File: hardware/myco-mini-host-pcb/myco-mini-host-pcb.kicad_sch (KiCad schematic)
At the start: 34 parts, among them J1 Conn_01x17_Female, J2 Conn_01x17_Female, Q1 AO3401A, Q2 AO3401A, Q3 AO3401A, Q4 AO3401A, SW1 DM-04-V, SW2 TS-1187A-B-A-B, U1 XC9145B33CMR-G, U2 SHT41-AD1B-R2, U3 BH1750FVI-TR, U4 MAX40203AUK+T

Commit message: fix: boost toujours actif (CE->VDD_NRF), modeles 3D, regles JLCPCB
- CE du XC9145 cable en dur sur VDD_NRF au lieu d'une GPIO : le boost
  alimente maintenant le nRF54 lui-meme, plus aucun scenario ou le
  firmware voudrait legitimement le couper (couperait sa propre
  alim) - supprime aussi le risque de brick si cette GPIO avait ete
  mise a l'etat bas par erreur
- R6 (pull-down CE) retire, plus necessaire - le tie direct satisfait
  deja l'exigence datasheet "ne pas laisser CE flottant"
- P1.05 redevient libre (broche J1 pin13)
- fix regression : label C2 revenu sur VDD_NRF au lieu de VOUT_3V3
  entre deux etapes precedentes (cause non identifiee avec certitude,
  isole aux 8 autres renommages de la meme tache qui etaient intacts)
- chemins de modeles 3D corriges sur les 8 footprints custom
  (${KIPRJMOD}/libs/... au lieu d'un chemin absolu casse)
- modeles 3D ajoutes pour U1 (XC9145, generique SOT-23-5 - LCSC n'a
  aucun modele pour ce package) et D1 (LED RGB 5050-6, meme raison)
- regles de conception resserrees pour matcher les minimums JLCPCB
  (min_clearance, min_via_diameter, min_via_annular_width,
  min_hole_to_hole) - geometrie actuelle du board deja conforme,
  DRC toujours propre apres resserrement
- placement/routage PCB (travail manuel utilisateur)

Co-Authored-By: Claude Sonnet 5 <noreply@anthropic.com>
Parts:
- removed R6: 100k, Resistor_SMD:R_0603_1608Metric, symbol Device:R
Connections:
- net VDD_NRF: now also U1.1 (CE)
- net P1_05_BOOST_EN: no longer names the net of J1.13 (Pin_13)
- net P1_05_BOOST_EN: no longer U1.1 (CE)
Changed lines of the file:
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@@
 	(wire
 		(pts
-			(xy 250.19 66.04) (xy 250.19 62.23)
-		)
-		(stroke
-			(width 0)
-			(type default)
-		)
-	)
-	(wire
-		(pts
 			(xy 34.29 69.85) (xy 30.48 69.85)
 		)
@@
 	(wire
 		(pts
+			(xy 34.29 107.95) (xy 30.48 107.95)
+		)
+		(stroke
+			(width 0)
+			(type default)
+		)
+	)
+	(wire
+		(pts
 			(xy 360.68 154.94) (xy 364.49 154.94)
 		)
@@
 	(wire
 		(pts
-			(xy 250.19 73.66) (xy 250.19 77.47)
-		)
-		(stroke
-			(width 0)
-			(type default)
-		)
-	)
-	(wire
-		(pts
 			(xy 370.84 250.19) (xy 367.03 250.19)
 		)
@@
 	(wire
 		(pts
-			(xy 34.29 100.33) (xy 30.48 100.33)
-		)
-		(stroke
-			(width 0)
-			(type default)
-		)
-	)
-	(wire
-		(pts
 			(xy 350.52 246.38) (xy 350.52 242.57)
 		)
@@
 		)
 	)
-	(wire
-		(pts
-			(xy 34.29 107.95) (xy 30.48 107.95)
-		)
-		(stroke
-			(width 0)
-			(type default)
-		)
-	)
 	(label "SENSOR_3V3"
 		(at 129.54 92.71 0)
@@
 		)
 	)
-	(label "P1_10_SDA"
-		(at 22.86 74.93 0)
+	(label "VDD_NRF"
+		(at 199.39 31.75 0)
 		(effects
 			(font
@@
 		)
 	)
-	(label "LED_B_NODE"
-		(at 367.03 246.38 0)
+	(label "P1_10_SDA"
+		(at 22.86 74.93 0)
 		(effects
 			(font
@@
 		)
 	)
-	(label "P1_05_BOOST_EN"
-		(at 250.19 62.23 0)
+	(label "LED_B_NODE"
+		(at 367.03 246.38 0)
 		(effects
 			(font
@@
 		)
 	)
-	(label "P1_05_BOOST_EN"
+	(label "VDD_NRF"
 		(at 236.22 41.91 0)
 		(effects
@@
 		)
 	)
-	(label "P1_05_BOOST_EN"
-		(at 30.48 100.33 0)
-		(effects
-			(font
-				(size 1.27 1.27)
-			)
-			(justify left bottom)
-		)
-	)
 	(label "P2_06_LED_B"
 		(at 16.51 195.58 0)
@@
 		)
 	)
+	(label "P1_08_SOIL_SW"
+		(at 30.48 107.95 0)
+		(effects
+			(font
+				(size 1.27 1.27)
+			)
+			(justify left bottom)
+		)
+	)
 	(label "VDD_PROT"
 		(at 165.1 69.85 0)
@@
 		)
 	)
-	(label "VDD_NRF"
-		(at 199.39 31.75 0)
-		(effects
-			(font
-				(size 1.27 1.27)
-			)
-			(justify left bottom)
-		)
-	)
 	(label "P2_03_DIP3"
 		(at 30.48 203.2 0)
@@
 		)
 	)
-	(label "P1_08_SOIL_SW"
-		(at 30.48 107.95 0)
-		(effects
-			(font
-				(size 1.27 1.27)
-			)
-			(justify left bottom)
-		)
-	)
 	(symbol
 		(lib_id "power:GND")
@@
 	(symbol
 		(lib_id "Device:R")
-		(at 250.19 69.85 0)
-		(unit 1)
-		(body_style 1)
-		(exclude_from_sim no)
-		(in_bom yes)
-		(on_board yes)
-		(in_pos_files yes)
-		(dnp no)
-		(property "Reference" "R6"
-			(at 250.19 63.85 0)
-			(show_name no)
-			(do_not_autoplace no)
-			(effects
-				(font
-					(size 1.27 1.27)
-				)
-			)
-		)
-		(property "Value" "100k"
-			(at 250.19 75.85 0)
-			(show_name no)
-			(do_not_autoplace no)
-			(effects
-				(font
-					(size 1.27 1.27)
-				)
-			)
-		)
-		(property "Footprint" "Resistor_SMD:R_0603_1608Metric"
-			(at 250.19 69.85 0)
-			(hide yes)
-			(show_name no)
-			(do_not_autoplace no)
-			(effects
-				(font
-					(size 1.27 1.27)
-				)
-			)
-		)
-		(property "Datasheet" ""
-			(at 250.19 69.85 0)
-			(show_name no)
-			(do_not_autoplace no)
-			(effects
-				(font
-					(size 1.27 1.27)
-				)
-			)
-		)
-		(property "Description" ""
-			(at 250.19 69.85 0)
-			(show_name no)
-			(do_not_autoplace no)
-			(effects
-				(font
-					(size 1.27 1.27)
-				)
-			)
-		)
-		(property "Note" "CE pull-down - datasheet: do not leave CE open"
-			(at 250.19 69.85 0)
-			(hide yes)
-			(show_name no)
-			(do_not_autoplace no)
-			(effects
-				(font
-					(size 1.27 1.27)
-				)
-			)
-		)
-		(pin "1"
-		)
-		(pin "2"
-		)
-		(instances
-			(project "myco-mini-host-pcb"
-				(path "/b1969cb4-f84b-4d7e-8508-ab863aa656b2"
-					(reference "R6")
-					(unit 1)
-				)
-			)
-		)
-	)
-	(symbol
-		(lib_id "Device:R")
 		(at 412.75 114.3 0)
 		(unit 1)
@@
 					(unit 1)
 				)
-			)
-		)
-	)
-	(symbol
-		(lib_id "power:GND")
-		(at 250.19 77.47 0)
-		(unit 1)
-		(body_style 1)
-		(exclude_from_sim no)
-		(in_bom yes)
-		(on_board yes)
-		(in_pos_files yes)
-		(dnp no)
-		(property "Reference" "#PWR10"
-			(at 250.19 83.47 0)
-			(hide yes)
-			(show_name no)
-			(do_not_autoplace no)
-			(effects
-				(font
-					(size 1.27 1.27)
-				)
-			)
-		)
-		(property "Value" "GND"
-			(at 250.19 81.47 0)
-			(show_name no)
-			(do_not_autoplace no)
-			(effects
-				(font
-					(size 1.27 1.27)
-				)
-			)
-		)
-		(property "Footprint" ""
-			(at 250.19 77.47 0)
-			(hide yes)
-			(show_name no)
-			(do_not_autoplace no)
-			(effects
-				(font
-					(size 1.27 1.27)
-				)
-			)
-		)
-		(property "Datasheet" ""
-			(at 250.19 77.47 0)
-			(show_name no)
-			(do_not_autoplace no)
-			(effects
-				(font
-					(size 1.27 1.27)
-				)
-			)
-		)
-		(property "Description" ""
-			(at 250.19 77.47 0)
-			(show_name no)
-			(do_not_autoplace no)
-			(effects
-				(font
-					(size 1.27 1.27)
-				)
-			)
-		)
-		(pin "1"
-		)
-		(instances
-			(project "myco-mini-host-pcb"
-				(path "/b1969cb4-f84b-4d7e-8508-ab863aa656b2"
-					(reference "#PWR10")
-					(unit 1)
-				)

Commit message: chore: snapshot avant corrections audit #2 (passe manuelle utilisateur)
Etat du schema et du PCB apres la passe manuelle de l'utilisateur
(alignement des textes/labels pour qu'ils ne chevauchent plus les
symboles, placement/routage PCB), avant d'appliquer les corrections
remontees par le second audit Opus 5.

Point de retour propre pour les corrections a venir :
- Q1 (protection inversion polarite) oriente a l'envers
- pas de decouplage sur SENSOR_3V3
- pas de pull-up sur P1_12_SENSOR_EN (Q3/Q4 flottants au boot)
- LED rouge/vert croisees, stubs I2C orphelins
- BOM obsolete (R6 fantome, commentaire R11/R12)
- VDD_NRF mal nomme (n'alimente plus le nRF54)

Co-Authored-By: Claude Sonnet 5 <noreply@anthropic.com>
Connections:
- net LED_B_NODE: no longer names the net of D1.1 (B), R9.1
- net LED_G_NODE: no longer names the net of D1.3 (G), R8.1
- net LED_R_NODE: no longer names the net of D1.2 (R), R7.1
- no-connect marks 0 -> 15
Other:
- note removed: "J1 = recepteur breakout J1 'GPIO_L' (1x17, 2.54mm)"
- note removed: "J2 = recepteur breakout J4 'GPIO_R' (1x17, 2.54mm)"
- note removed: "Pins headers non utilisees dans ce brouillon = laissees non cablees (GPIO libres, voir docs/host-pcb-design-brief.md)"
- moved on the sheet: D1, J1, J2, L1, R7, R8, R9, SW1

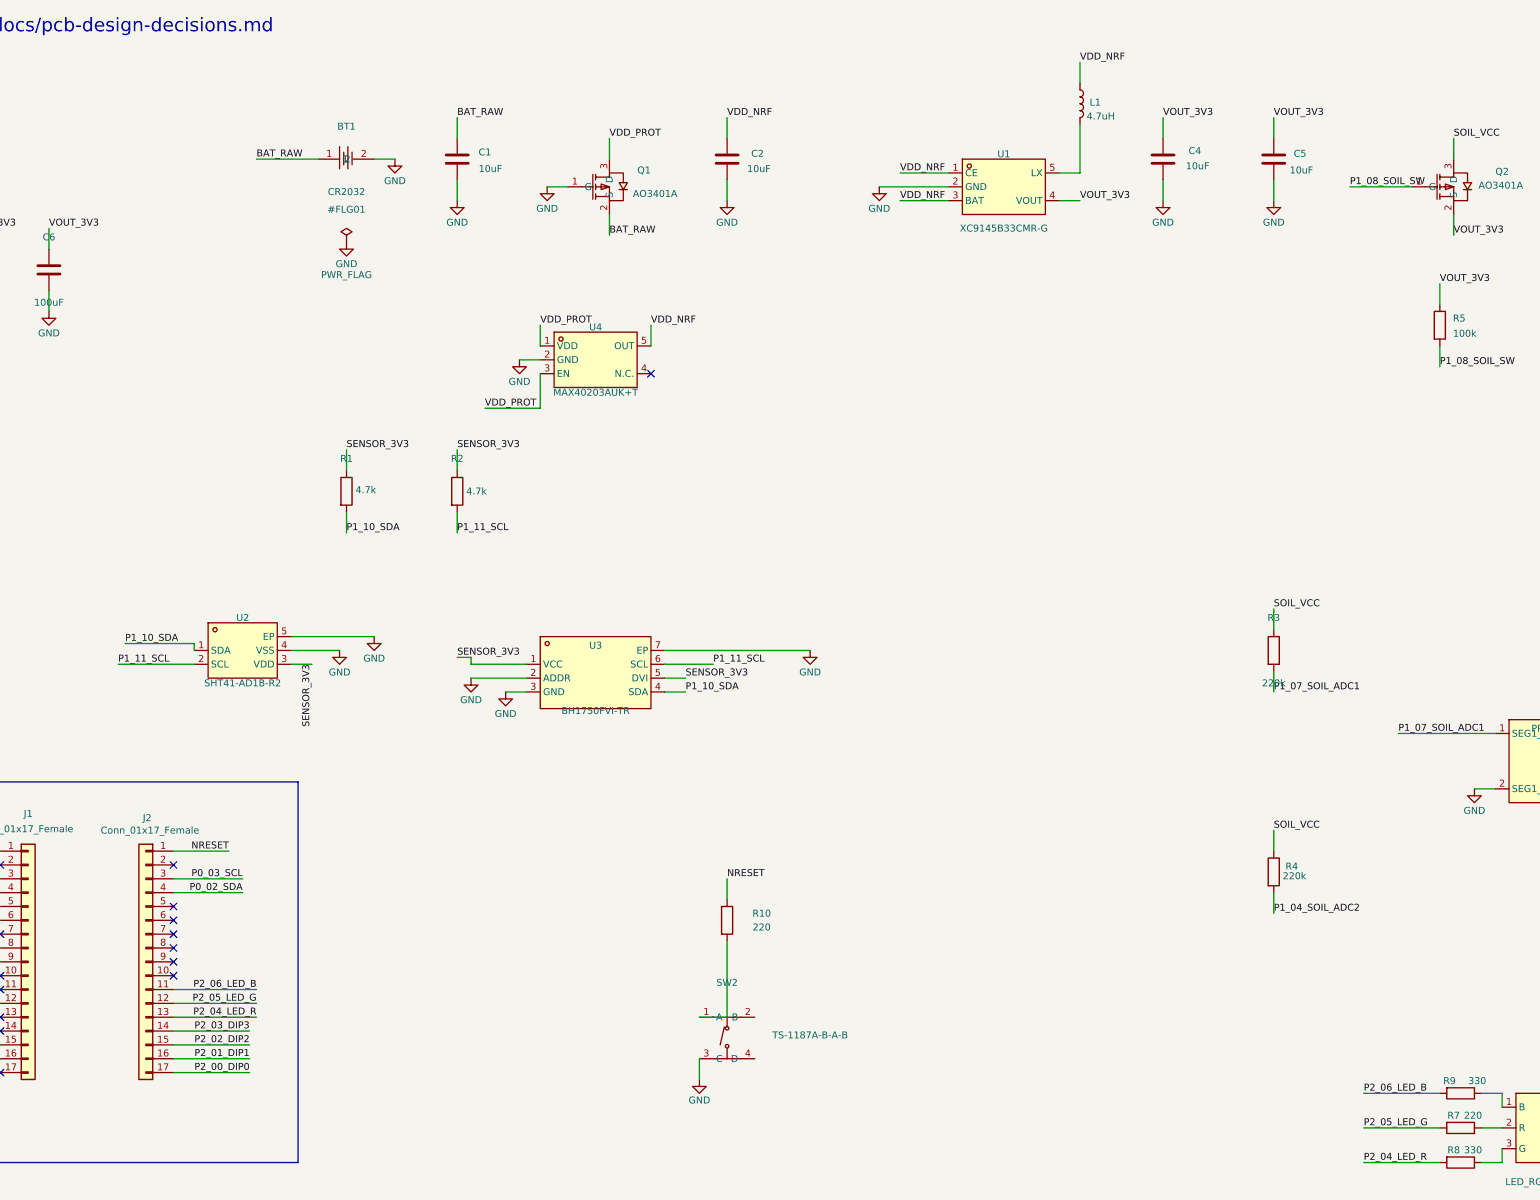
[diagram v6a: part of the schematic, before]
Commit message: fix: Q1 oriente a l'envers (aucune protection inversion), decouplage, garde-fous
Corrections du second audit Opus 5. Schema uniquement, le PCB reste a
l'utilisateur.

CRITIQUE - Q1 (protection inversion polarite) etait cable a l'envers :
  S=BAT_RAW / D=VDD_PROT, soit le motif "load switch" de Q2/Q3/Q4 (correct
  pour EUX, faux ici). Sur un P-FET la diode de corps a anode=Drain : avec
  la Source cote pile, une pile inseree a l'envers laisse cette diode
  PASSANTE, donc zero protection, et U4 (max absolu -0.3V) verrait ~-2.3V.
  Repere decisif : dans un montage correct la diode de corps conduit en
  fonctionnement NORMAL (elle amorce la charge, le canal la court-circuite
  ensuite) et ne bloque qu'a l'inversion. Corrige en D=BAT_RAW / S=VDD_PROT
  (echange des deux labels, aucune modif de geometrie). Brochage AO3401A
  reverifie sur datasheet (1=G, 2=S, 3=D). NB: le brief sec.4 contient
  toujours la meme erreur ("Source -> CR2032+"), d'ou le passage au travers
  du premier audit qui validait la conformite au brief, pas la physique.

Autres corrections :
- C7/C8 (100nF) + C9 (1uF) sur SENSOR_3V3 : le rail commute par Q3 n'avait
  aucune capacite locale, tout le decouplage etant reste en amont sur
  VOUT_3V3. ROHM specifie 0.1uF sur le VCC du BH1750, Sensirion l'exige
  pour le SHT4x, et ce rail se recharge depuis zero a chaque mesure.
- R13 (100k) sur P1_12_SENSOR_EN : les grilles de Q3/Q4 flottaient au boot
  (boost desormais toujours actif => VOUT_3V3 vivant avant que la GPIO ne
  sorte de haute impedance). Meme role que R5 pour Q2.
- LED rouge/vert : les noms de net etaient croises par rapport aux puces
  reellement atteintes. Valeurs des resistances deja correctes par couleur
  (220R sur le rouge), donc seuls les noms bougent.
- VDD_NRF -> BOOST_IN : ce net n'alimente plus le nRF54 depuis que J1 pin9
  est passe sur VOUT_3V3, c'est le rail d'entree du boost.
- Stubs I2C orphelins P0_02_SDA / P0_03_SCL supprimes, remplaces par des
  no-connect comme les autres br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
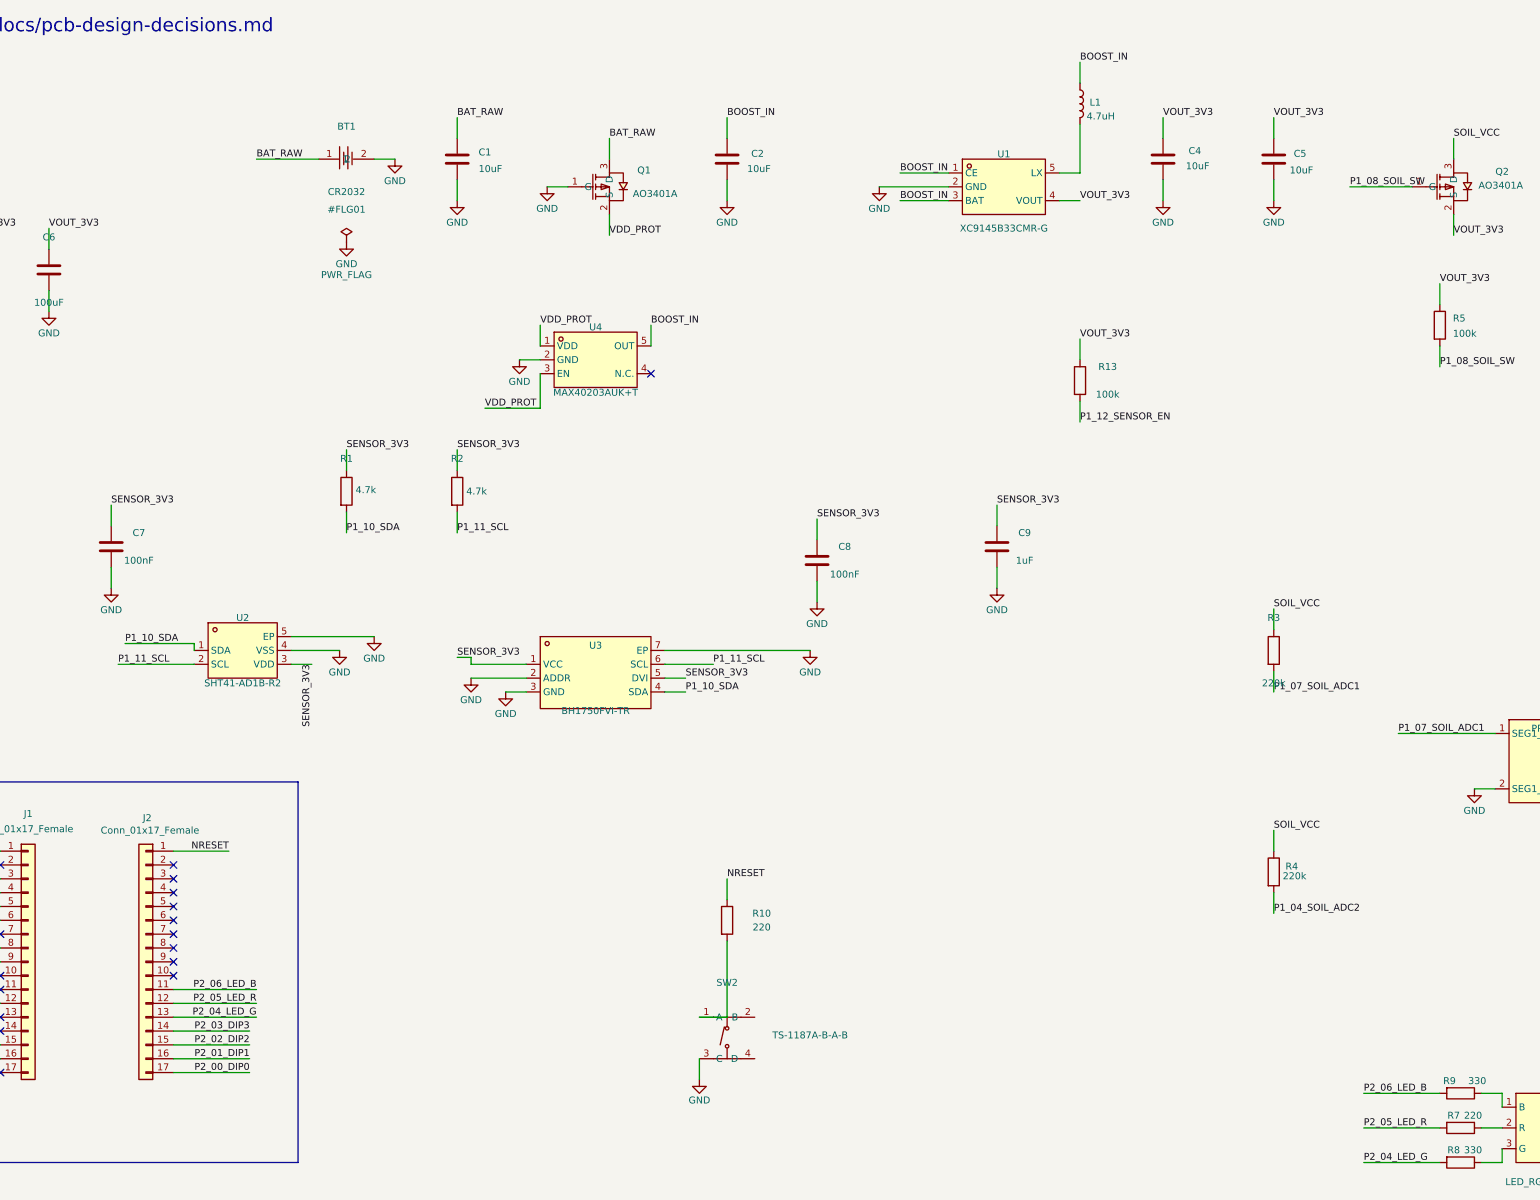
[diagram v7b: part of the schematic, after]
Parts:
- added C7, C8: 100nF, Capacitor_SMD:C_0603_1608Metric, symbol Device:C
- added C9: 1uF, Capacitor_SMD:C_0603_1608Metric, symbol Device:C
- added R13: 100k, Resistor_SMD:R_0603_1608Metric, symbol Device:R
- Q1: Note Reverse polarity protect ONLY: S=BAT_RAW D=VDD_PROT G=GND. 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 -> Reverse polarity protection: D=BAT_RAW S=VDD_PROT G=GND. Or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
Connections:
- net BAT_RAW: now also Q1.3 (D); no longer Q1.2 (S)
- net GND: now also C7.2, C8.2, C9.2
- net P1_12_SENSOR_EN: now also R13.2
- net SENSOR_3V3: now also C7.1, C8.1, C9.1
- net VDD_PROT: now also Q1.2 (S); no longer Q1.3 (D)
- net VOUT_3V3: now also R13.1
- net P0_02_SDA: no longer names the net of J2.4 (Pin_4)
- net P0_03_SCL: no longer names the net of J2.3 (Pin_3)
- net P2_04_LED_R renamed P2_04_LED_G
- net P2_05_LED_G renamed P2_05_LED_R
- net VDD_NRF renamed BOOST_IN
- no-connect marks 15 -> 17
